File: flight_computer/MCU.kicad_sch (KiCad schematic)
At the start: 1 part, among them U2 STM8S007C8T6

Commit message: MCU circuit started
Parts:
- added C1: 100nF, Capacitor_SMD:C_0402_1005Metric, symbol Device:C
- added C6: 1uF, symbol Device:C
- added C7, C8: 33pF, Capacitor_SMD:C_0402_1005Metric, symbol Device:C
- added J2: Conn_02x05_Counter_Clockwise, symbol Connector_Generic:Conn_02x05_Counter_Clockwise
- added R1: 1M, Resistor_SMD:R_0402_1005Metric, symbol Device:R
- added SW2: SW_Push, Button_Switch_THT:SW_PUSH_6mm, symbol Switch:SW_Push
- added Y1: 12MHz, Crystal:Crystal_SMD_3225-4Pin_3.2x2.5mm, symbol Device:Crystal_GND24
- U2: value STM8S007C8T6 -> STM8S007C8T6TR; Manufacturer PN (none) -> STM8S007C8T6TR; Supplier (none) -> Digikey; Supplier PN (none) -> 497-18848-1-ND
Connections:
- net NRST: now reaches U2.1 (NRST)
- net NRST: now also C1.1, J2.1 (Pin_1), R1.2, SW2.1
- net at U2.2 (PA1/OSCIN): now also C7.2, Y1.1
- net at U2.3 (PA2/OSCOUT): now also C8.1, Y1.3
- net SWIM: now reaches U2.42 (PD1)
- net SWIM: now also J2.2 (Pin_2)
- net 3V3A: now reaches U2.13 (VDDA)
- net GND: now reaches U2.14 (VSSA)
- net GND: now also U2.31 (VSSIO_2), U2.4 (VSSIO_1), U2.5 (VSS), C1.2, C6.2, C7.1, C8.2, J2.3 (Pin_3), J2.8 (Pin_8), SW2.2, Y1.2, Y1.4
- net 3V3D: now reaches U2.32 (VDDIO_2)
- net 3V3D: now also U2.7 (VDD), U2.8 (VDDIO_1), J2.4 (Pin_4), J2.7 (Pin_7), R1.1
- net at U2.6 (VCAP): now also C6.1
- no-connect marks 0 -> 4
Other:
- note added: "5V"
- note added: "Choose CX1 = CX2 = CX Assume Cstray = 3pF CL = 20pF (crystal datasheet) CX = 2(CL-Cstray) = 2(20-3) = 34pF Choose 33pF for E12 standard"
- note added: "SWCLK"
- note added: "SWDIO"
- moved on the sheet: U2A, U2B

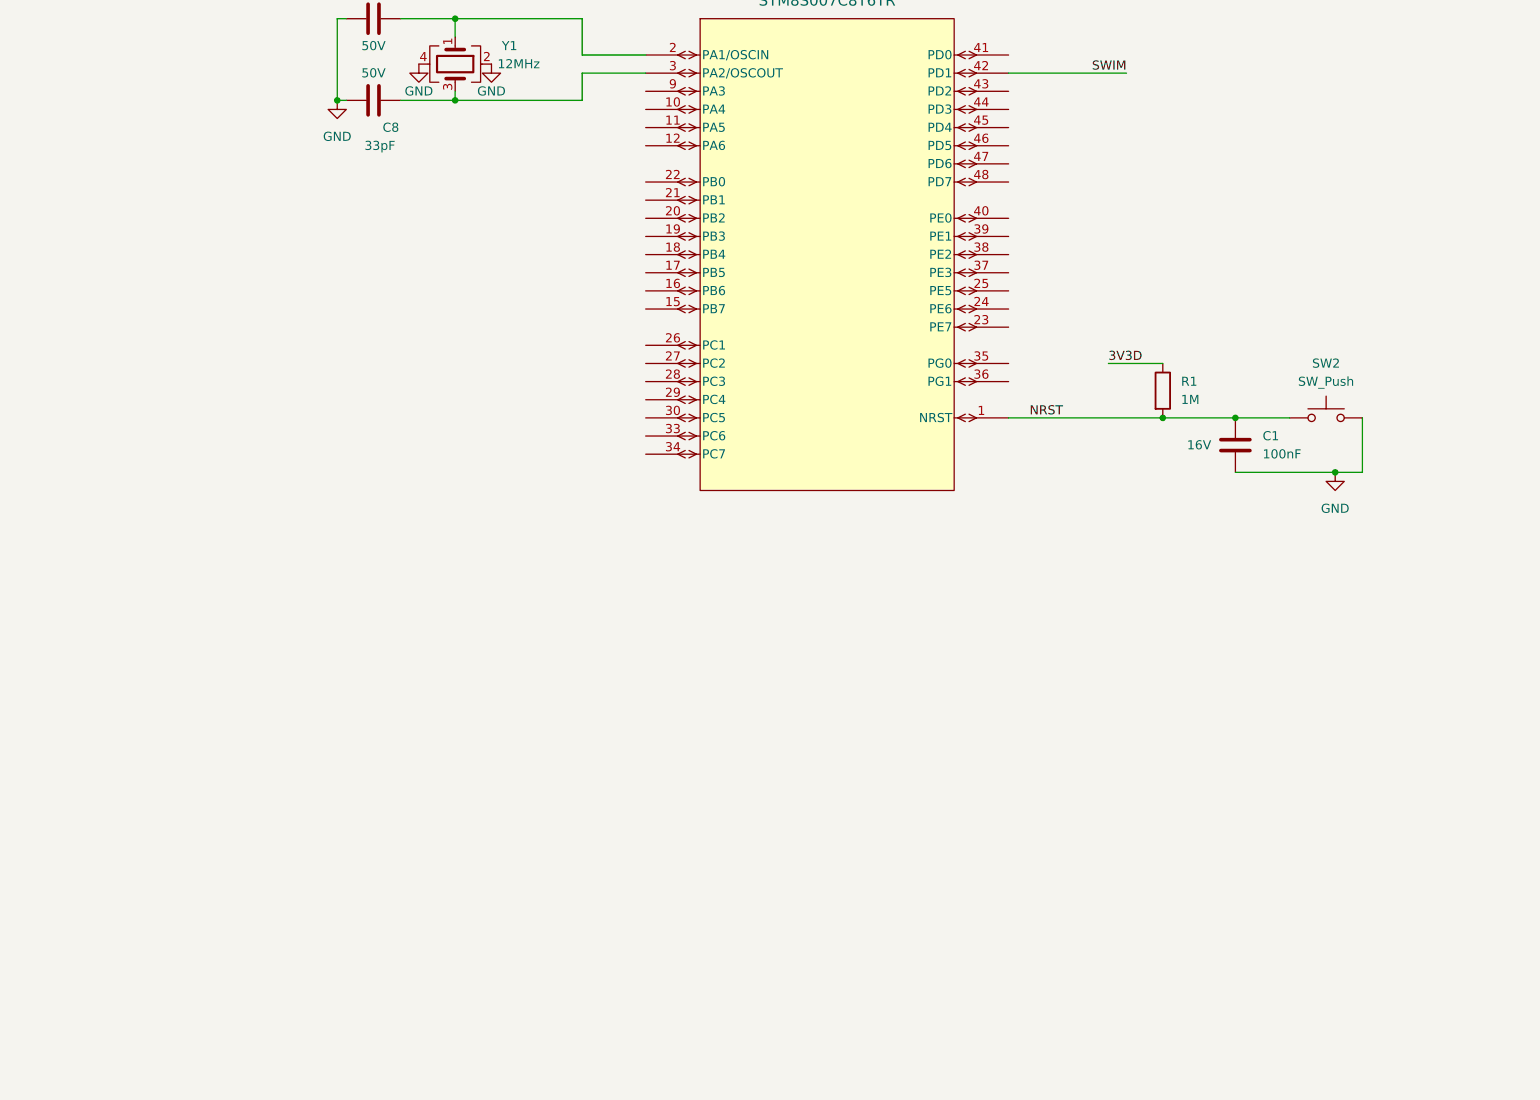
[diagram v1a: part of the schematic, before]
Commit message: Buzzer, LEDs, added actual components for current sensing and others I had missed
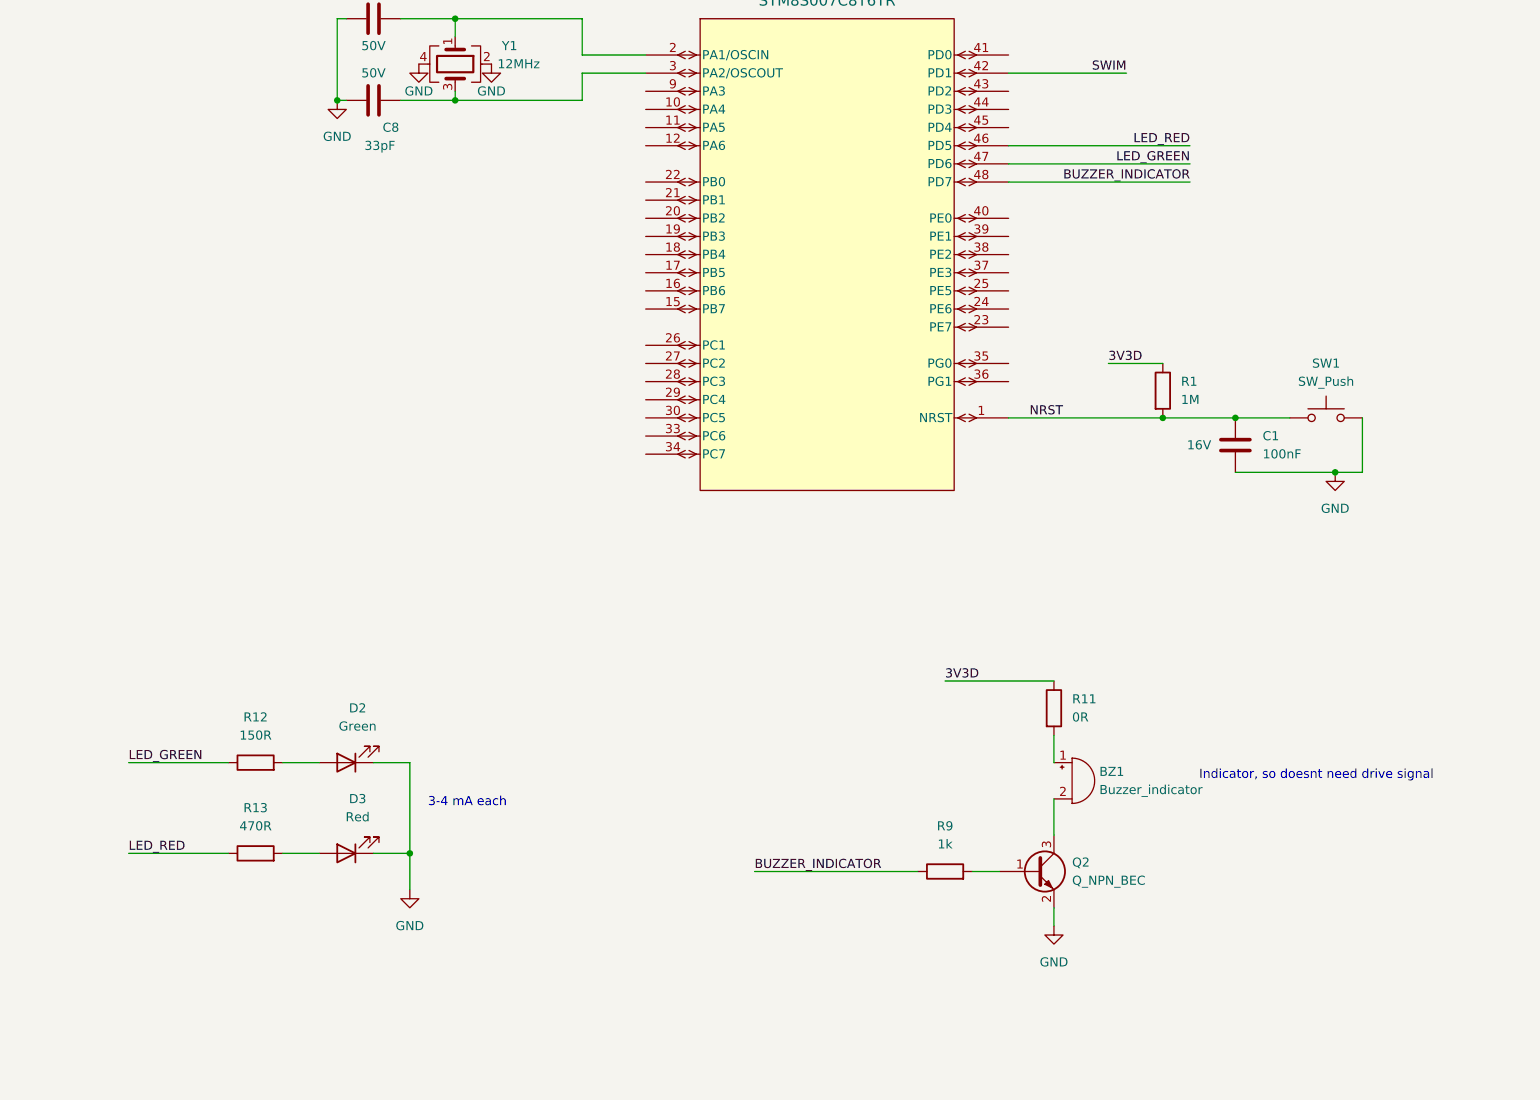
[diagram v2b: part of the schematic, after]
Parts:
- removed SW2: SW_Push, Button_Switch_THT:SW_PUSH_6mm, symbol Switch:SW_Push
- added BZ1: Buzzer_indicator, my_footprints:buzzer_Dia9.2mm_P5mm, symbol Device:Buzzer
- added D2: Green, LED_SMD:LED_0805_2012Metric, symbol Device:LED
- added D3: Red, LED_SMD:LED_0805_2012Metric, symbol Device:LED
- added Q2: Q_NPN_BEC, Package_TO_SOT_SMD:SOT-23-3, symbol Device:Q_NPN_BEC
- added R11: 0R, Resistor_SMD:R_0402_1005Metric, symbol Device:R
- added R12: 150R, Resistor_SMD:R_0402_1005Metric, symbol Device:R
- added R13: 470R, Resistor_SMD:R_0402_1005Metric, symbol Device:R
- added R9: 1k, Resistor_SMD:R_0402_1005Metric, symbol Device:R
- added SW1: SW_Push, my_footprints:KMR2_1, symbol Switch:SW_Push
- C6: footprint (none) -> Capacitor_SMD:C_0402_1005Metric; Manufacturer PN (none) -> CL05A105KA5NQNC; Supplier (none) -> JLC; Supplier PN (none) -> C52923
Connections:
- net 3V3D: now also R11.1
- net GND: now also D2.1 (K), D3.1 (K), Q2.2 (E), SW1.2
- net NRST: now also SW1.1
- net LED_RED: now reaches U2.46 (PD5)
- net LED_RED: now also R13.1
- net LED_GREEN: now reaches U2.47 (PD6)
- net LED_GREEN: now also R12.1
- net BUZZER_INDICATOR: now reaches U2.48 (PD7)
- net BUZZER_INDICATOR: now also R9.1
- new net: BZ1.1 (-), R11.2
- new net: D3.2 (A), R13.2
- new net: BZ1.2 (+), Q2.3 (C)
- new net: Q2.1 (B), R9.2
- new net: D2.2 (A), R12.2
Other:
- note added: "3-4 mA each"
- note added: "Indicator, so doesnt need drive signal"

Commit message: Button
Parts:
- added J3: Micro_SD_Card, symbol Connector:Micro_SD_Card
- added R1: 1M, Resistor_SMD:R_0402_1005Metric, symbol Device:R
- added SW2: SW_Push, my_footprints:KMR2_1, symbol Switch:SW_Push
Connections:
- net 3V3D: now also SW2.2
- net GND: now also R1.2
- net BUTTON: now reaches U2.45 (PD4)
- net BUTTON: now also R1.1, SW2.1
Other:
- moved on the sheet: D2, D3, R12, R13

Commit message: SD card
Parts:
- removed J3: Micro_SD_Card, symbol Connector:Micro_SD_Card
- added J3: MEM2061-01-188-00-A_REVA, my_footprints:MEM2061-01-188-00-A, symbol my_library:MEM2061-01-188-00-A_REVA
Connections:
- net 3V3D: now also J3.4 (VDD)
- net GND: now also J3.11 (GND), J3.12 (GND__1), J3.6 (VSS)
- net SPI_NSS: now reaches U2.25 (PE5)
- net SPI_NSS: now also J3.2 (CD/DAT3)
- net SPI_SCK: now reaches U2.30 (PC5)
- net SPI_SCK: now also J3.5 (CLK)
- net SPI_MOSI: now reaches U2.33 (PC6)
- net SPI_MOSI: now also J3.3 (CMD)
- net SPI_MISO: now reaches U2.34 (PC7)
- net SPI_MISO: now also J3.7 (DAT0)
- no-connect marks 4 -> 8

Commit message: PRessure sensor circuit
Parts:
- added R15, R16: 4.7k, Resistor_SMD:R_0402_1005Metric, symbol Device:R
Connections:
- net 3V3D: now also R15.1, R16.1
- net SDA: now reaches U2.17 (PB5)
- net SDA: now also R16.2
- net SCL: now reaches U2.18 (PB4)
- net SCL: now also R15.2
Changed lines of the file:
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@@
   (junction (at 81.28 154.94) (diameter 0) (color 0 0 0 0)
   )
+  (junction (at 236.22 140.97) (diameter 0) (color 0 0 0 0)
+  )
   (junction (at 207.01 203.2) (diameter 0) (color 0 0 0 0)
   )
@@
   (junction (at 110.49 154.94) (diameter 0) (color 0 0 0 0)
   )
+  (junction (at 236.22 129.54) (diameter 0) (color 0 0 0 0)
+  )
   (junction (at 334.01 78.74) (diameter 0) (color 0 0 0 0)
   )
@@
   )
   (junction (at 340.36 161.29) (diameter 0) (color 0 0 0 0)
+  )
+  (junction (at 246.38 138.43) (diameter 0) (color 0 0 0 0)
   )
   (junction (at 106.68 250.19) (diameter 0) (color 0 0 0 0)
@@
     (stroke (width 0) (type default))
   )
+  (wire (pts (xy 232.41 140.97) (xy 236.22 140.97))
+    (stroke (width 0) (type default))
+  )
+  (wire (pts (xy 236.22 140.97) (xy 257.81 140.97))
+    (stroke (width 0) (type default))
+  )
   (wire (pts (xy 248.92 105.41) (xy 248.92 110.49))
     (stroke (width 0) (type default))
@@
     (stroke (width 0) (type default))
   )
+  (wire (pts (xy 228.6 129.54) (xy 236.22 129.54))
+    (stroke (width 0) (type default))
+  )
   (wire (pts (xy 218.44 196.85) (xy 223.52 196.85))
     (stroke (width 0) (type default))
@@
     (stroke (width 0) (type default))
   )
+  (wire (pts (xy 246.38 138.43) (xy 257.81 138.43))
+    (stroke (width 0) (type default))
+  )
   (wire (pts (xy 238.76 161.29) (xy 257.81 161.29))
     (stroke (width 0) (type default))
@@
     (stroke (width 0) (type default))
   )
+  (wire (pts (xy 236.22 129.54) (xy 236.22 133.35))
+    (stroke (width 0) (type default))
+  )
   (wire (pts (xy 132.08 238.76) (xy 132.08 250.19))
     (stroke (width 0) (type default))
   )
+  (wire (pts (xy 246.38 130.81) (xy 246.38 129.54))
+    (stroke (width 0) (type default))
+  )
   (wire (pts (xy 113.03 233.68) (xy 127 233.68))
     (stroke (width 0) (type default))
@@
     (stroke (width 0) (type default))
   )
+  (wire (pts (xy 232.41 138.43) (xy 246.38 138.43))
+    (stroke (width 0) (type default))
+  )
   (wire (pts (xy 303.53 224.79) (xy 307.34 224.79))
     (stroke (width 0) (type default))
@@
   )
   (wire (pts (xy 334.01 60.96) (xy 349.25 60.96))
+    (stroke (width 0) (type default))
+  )
+  (wire (pts (xy 236.22 129.54) (xy 246.38 129.54))
     (stroke (width 0) (type default))
   )
@@
     (effects (font (size 1.27 1.27)) (justify right bottom))
   )
+  (label "3V3D" (at 228.6 129.54 0) (fields_autoplaced)
+    (effects (font (size 1.27 1.27)) (justify left bottom))
+  )
   (label "3V3D" (at 334.01 48.26 0) (fields_autoplaced)
     (effects (font (size 1.27 1.27)) (justify left bottom))
@@
   )
   (hierarchical_label "GND" (shape input) (at 71.12 154.94 180) (fields_autoplaced)
+    (effects (font (size 1.27 1.27)) (justify right))
+  )
+  (hierarchical_label "SCL" (shape output) (at 232.41 138.43 180) (fields_autoplaced)
+    (effects (font (size 1.27 1.27)) (justify right))
+  )
+  (hierarchical_label "SDA" (shape output) (at 232.41 140.97 180) (fields_autoplaced)
     (effects (font (size 1.27 1.27)) (justify right))
   )
@@
     )
   )
+  (symbol (lib_id "Device:R") (at 236.22 137.16 0) (unit 1)
+    (in_bom yes) (on_board yes) (dnp no) (fields_autoplaced)
+    (property "Reference" "R16" (at 238.76 135.89 0)
+      (effects (font (size 1.27 1.27)) (justify left))
+    )
+    (property "Value" "4.7k" (at 238.76 138.43 0)
+      (effects (font (size 1.27 1.27)) (justify left))
+    )
+    (property "Footprint" "Resistor_SMD:R_0402_1005Metric" (at 234.442 137.16 90)
+      (effects (font (size 1.27 1.27)) hide)
+    )
+    (property "Datasheet" "https://wmsc.lcsc.com/wmsc/upload/file/pdf/v2/lcsc/2206010045_UNI-ROYAL-Uniroyal-Elec-0402WGF4701TCE_C25900.pdf" (at 236.22 137.16 0)
+      (effects (font (size 1.27 1.27)) hide)
+    )
+    (property "Manufacturer PN" "0402WGF4701TCE" (at 236.22 137.16 0)
+      (effects (font (size 1.27 1.27)) hide)
+    )
+    (property "Supplier PN" "C25900" (at 236.22 137.16 0)
+      (effects (font (size 1.27 1.27)) hide)
+    )
+    (property "Supplier" "JLC" (at 236.22 137.16 0)
+      (effects (font (size 1.27 1.27)) hide)
+    )
+    (pin "1")
+    (pin "2")
+    (instances
+      (project "flight_computer"
+        (path "/89a81c02-14e9-456f-a334-ff69a24bd093/60625ff5-21c7-44a3-8ce9-cc38254a738b"
+          (reference "R16") (unit 1)
+        )
+      )
+    )
+  )
   (symbol (lib_id "Device:Buzzer") (at 317.5 212.09 0) (unit 1)
     (in_bom yes) (on_board yes) (dnp no) (fields_autoplaced)
@@
         )
       )
+    )
+  )
+  (symbol (lib_id "Device:R") (at 246.38 134.62 0) (unit 1)
+    (in_bom yes) (on_board yes) (dnp no) (fields_autoplaced)
+    (property "Reference" "R15" (at 248.92 133.35 0)
+      (effects (font (size 1.27 1.27)) (justify left))
+    )
+    (property "Value" "4.7k" (at 248.92 135.89 0)
+      (effects (font (size 1.27 1.27)) (justify left))
+    )
+    (property "Footprint" "Resistor_SMD:R_0402_1005Metric" (at 244.602 134.62 90)
+      (effects (font (size 1.27 1.27)) hide)
+    )
+    (property "Datasheet" "https://wmsc.lcsc.com/wmsc/upload/file/pdf/v2/lcsc/2206010045_UNI-ROYAL-Uniroyal-Elec-0402WGF4701TCE_C25900.pdf" (at 246.38 134.62 0)
+      (effects (font (size 1.27 1.27)) hide)
+    )
+    (property "Manufacturer PN" "0402WGF4701TCE" (at 246.38 134.62 0)
+      (effects (font (size 1.27 1.27)) hide)
+    )
+    (property "Supplier PN" "C25900" (at 246.38 134.62 0)
+      (effects (font (size 1.27 1.27)) hide)
+    )
+    (property "Supplier" "JLC" (at 246.38 134.62 0)
+      (effects (font (size 1.27 1.27)) hide)
+    )
+    (pin "1")
+    (pin "2")
+    (instances
+      (project "flight_computer"
+        (path "/89a81c02-14e9-456f-a334-ff69a24bd093/60625ff5-21c7-44a3-8ce9-cc38254a738b"
+          (reference "R15") (unit 1)
+        )
+      )

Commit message: Tidying up schematics and adding most missing sections (Not finished GPS)
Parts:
- C1: renamed from C6; Voltage (none) -> 25V
- U2: value STM8S007C8T6TR -> STM8S007C8T6; Manufacturer PN STM8S007C8T6TR -> (none); Supplier Digikey -> (none); Supplier PN 497-18848-1-ND -> (none)
- renumbered C7 to C2, C8 to C3, D2 to D1, D3 to D2, J2 to J1, J3 to J2, Q2 to Q1, R12 to R1, R13 to R2, R16 to R4, R15 to R5, R11 to R7, SW2 to SW1, SW1 to SW2
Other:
- note added: "Buttons + LEDs"
- note added: "Buzzer"
- note added: "Crystal osc"
- note added: "MCU"
- note added: "MCU power"
- note added: "Programming"
- note added: "SD Card"
- moved on the sheet: BZ1, C1, C2, C3, D1, D2, J1, J2, Q1, R1, R2, R4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
